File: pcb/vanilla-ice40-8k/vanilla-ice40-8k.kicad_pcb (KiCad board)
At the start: 6 copper layers, 50 x 50 mm, 109 parts, among them J11 QSH-060-01-L-D-A, J12 QSH-060-01-L-D-A, J8 Conn_01x02_Pin, U1 ICE40HX8K-CT256, U2 W25X40CLSN, U3 FT2232HQ, U4 93LCxxBxxOT, U5 TPS563252DRLR, U6 TPS563252DRLR, X1 SG-8101CE 100Mhz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

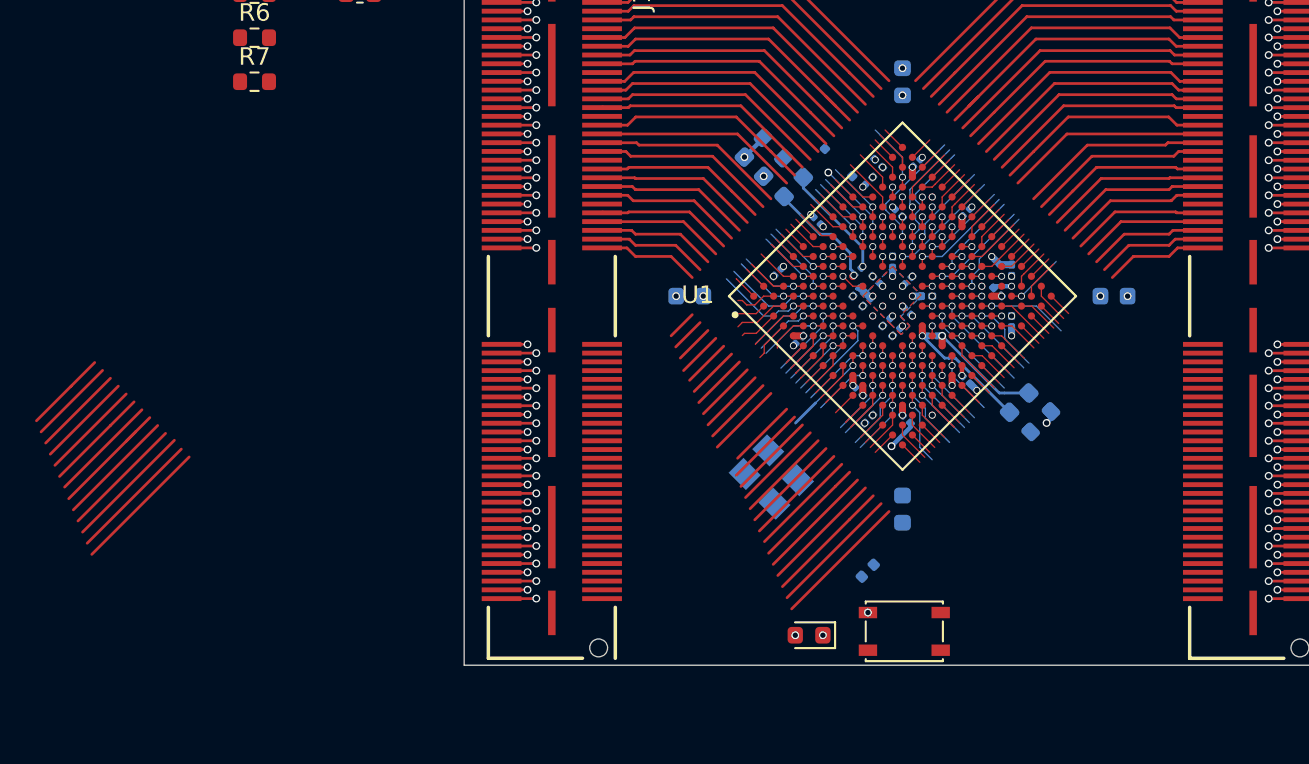
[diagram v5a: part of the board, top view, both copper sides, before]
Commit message: [hx8k][pcb] j1 and j2 mirroring fixed
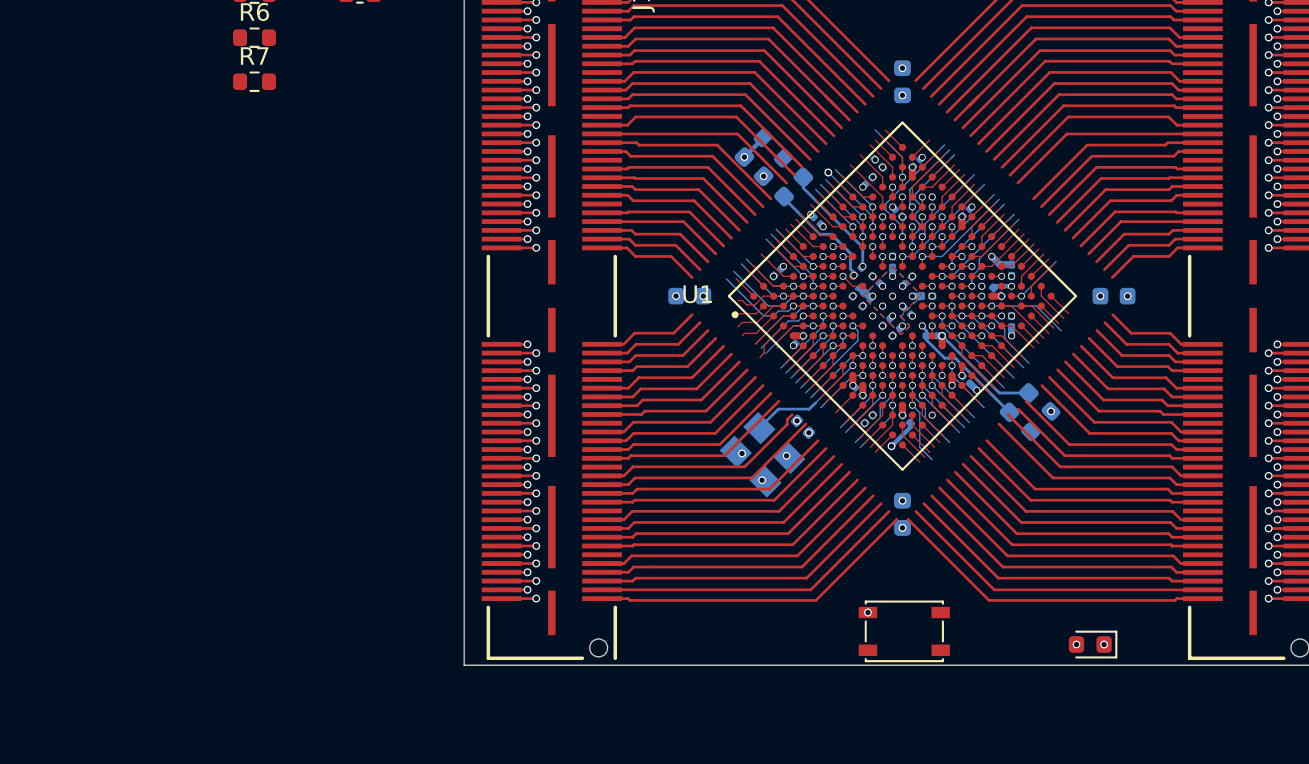
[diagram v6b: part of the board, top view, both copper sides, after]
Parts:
- removed D1: 1N4148WSF-7, Diode_SMD:D_SOD-323F
- moved USR1 16.0 mm to (85.7, 94.9)
- moved C1 9.00 mm to (69.3, 82.5), turned to 135 degrees
- moved X1 1.37 mm to (67.0, 84.0)
- moved C15 0.30 mm to (75.0, 87.4)
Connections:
- C13 pad 1: Net-(D1-K) -> +3V3
- U1 pad E12: Net-(D1-K) -> +3V3
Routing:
- net /IOB_53: track 1.40 -> 20.2 mm
- net /IOB_55: track 2.37 -> 20.6 mm
- net /IOB_57: track 1.40 -> 19.2 mm
- net /IOB_59: track 2.37 -> 19.6 mm
- net /IOB_61: track 1.40 -> 18.2 mm
- net /IOL_24A: track 1.40 -> 18.2 mm
- net /IOB_63: track 2.37 -> 18.5 mm
- net /IOB_60: track 2.37 -> 18.0 mm
- net /IOB_69: track 1.40 -> 16.6 mm
- net /IOB_71: track 2.37 -> 17.1 mm
- net /IOL_17B: track 1.40 -> 16.1 mm
- net unconnected-(J11-Pad110): track 14.1 -> 0.00 mm
- net /IOB_73: track 1.40 -> 15.4 mm
- net /IOB_75: track 1.40 -> 15.0 mm
- net /IOB_76: track 1.40 -> 14.5 mm
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
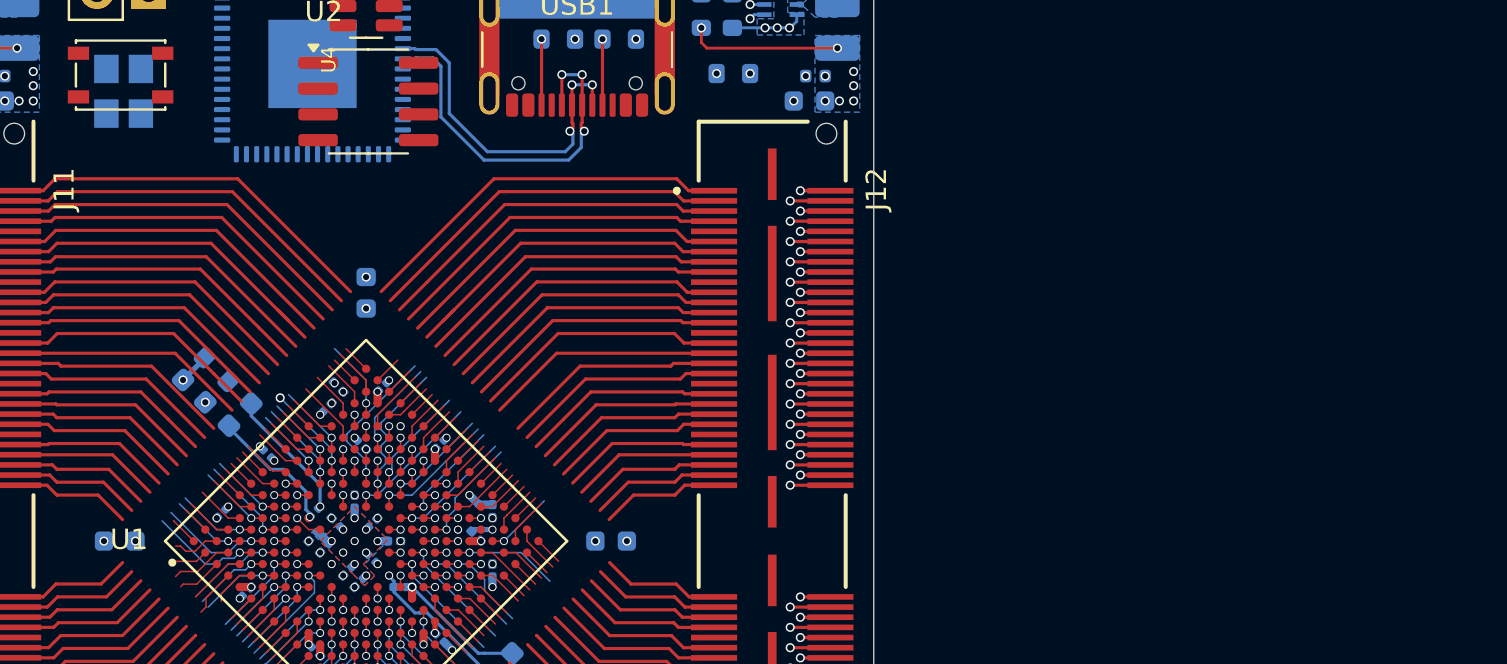
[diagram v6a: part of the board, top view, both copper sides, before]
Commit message: [hx8k][pcb] initial bga to j1 routing
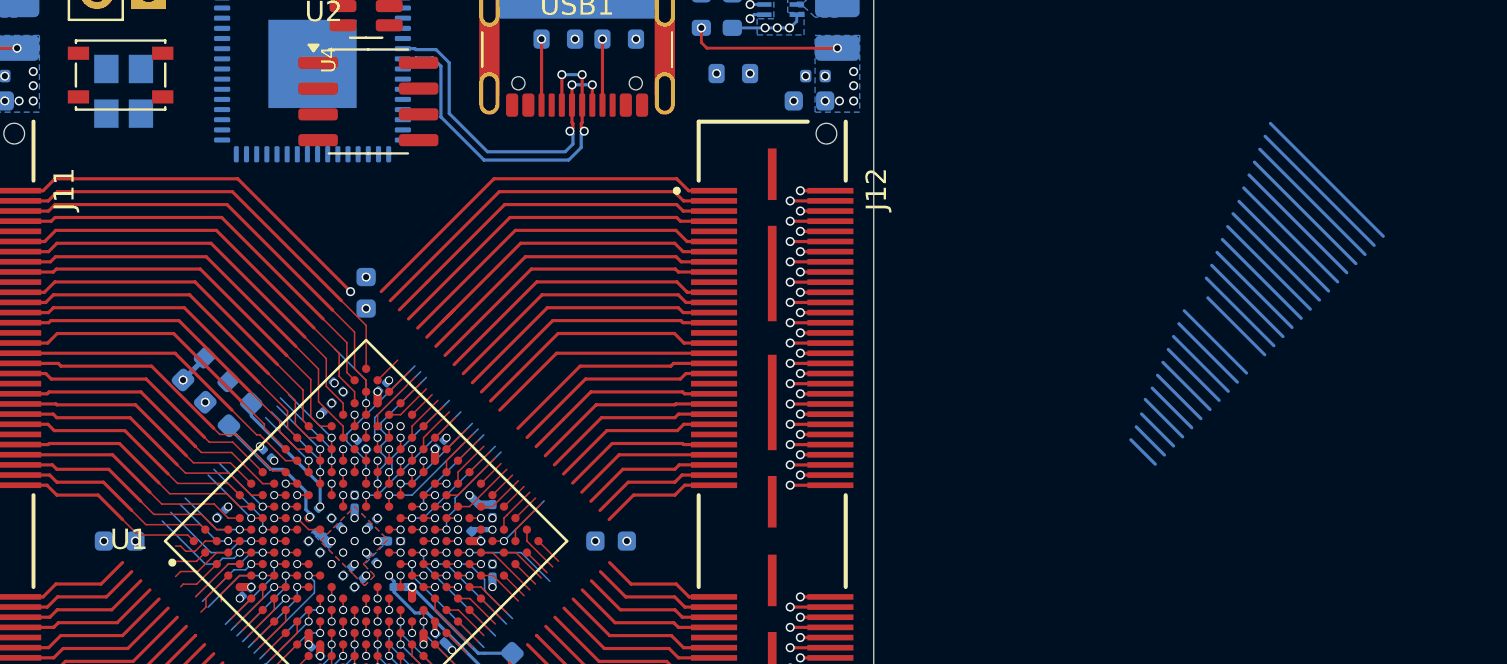
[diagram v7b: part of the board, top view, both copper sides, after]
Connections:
- J11 pad 42: /IOT_208 -> /IOT_207
- J11 pad 44: /IOT_207 -> /IOT_211
- J11 pad 46: /IOT_211 -> /IOT_208
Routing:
- net /IOT_170: track 23.5 -> 34.3 mm, vias 1 -> 2
- net /IOT_176: track 19.8 -> 29.8 mm
- net /IOT_169: track 20.1 -> 29.8 mm
- net /IOT_177: track 18.6 -> 27.9 mm
- net /IOT_171: track 19.2 -> 28.2 mm
- net /IOT_172: track 18.8 -> 27.3 mm
- net /IOT_182: track 17.4 -> 25.8 mm
- net /IOT_187: track 16.1 -> 24.1 mm
- net /IOT_178: track 19.4 -> 27.4 mm
- net /IOT_184: track 17.6 -> 25.3 mm
- net /IOT_186: track 14.9 -> 22.2 mm
- net /IOT_183: track 15.3 -> 22.2 mm
- net /IOT_207: track 11.7 -> 18.3 mm
- net /IOT_194: track 14.0 -> 20.5 mm
- net /IOT_203: track 13.3 -> 19.7 mm
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
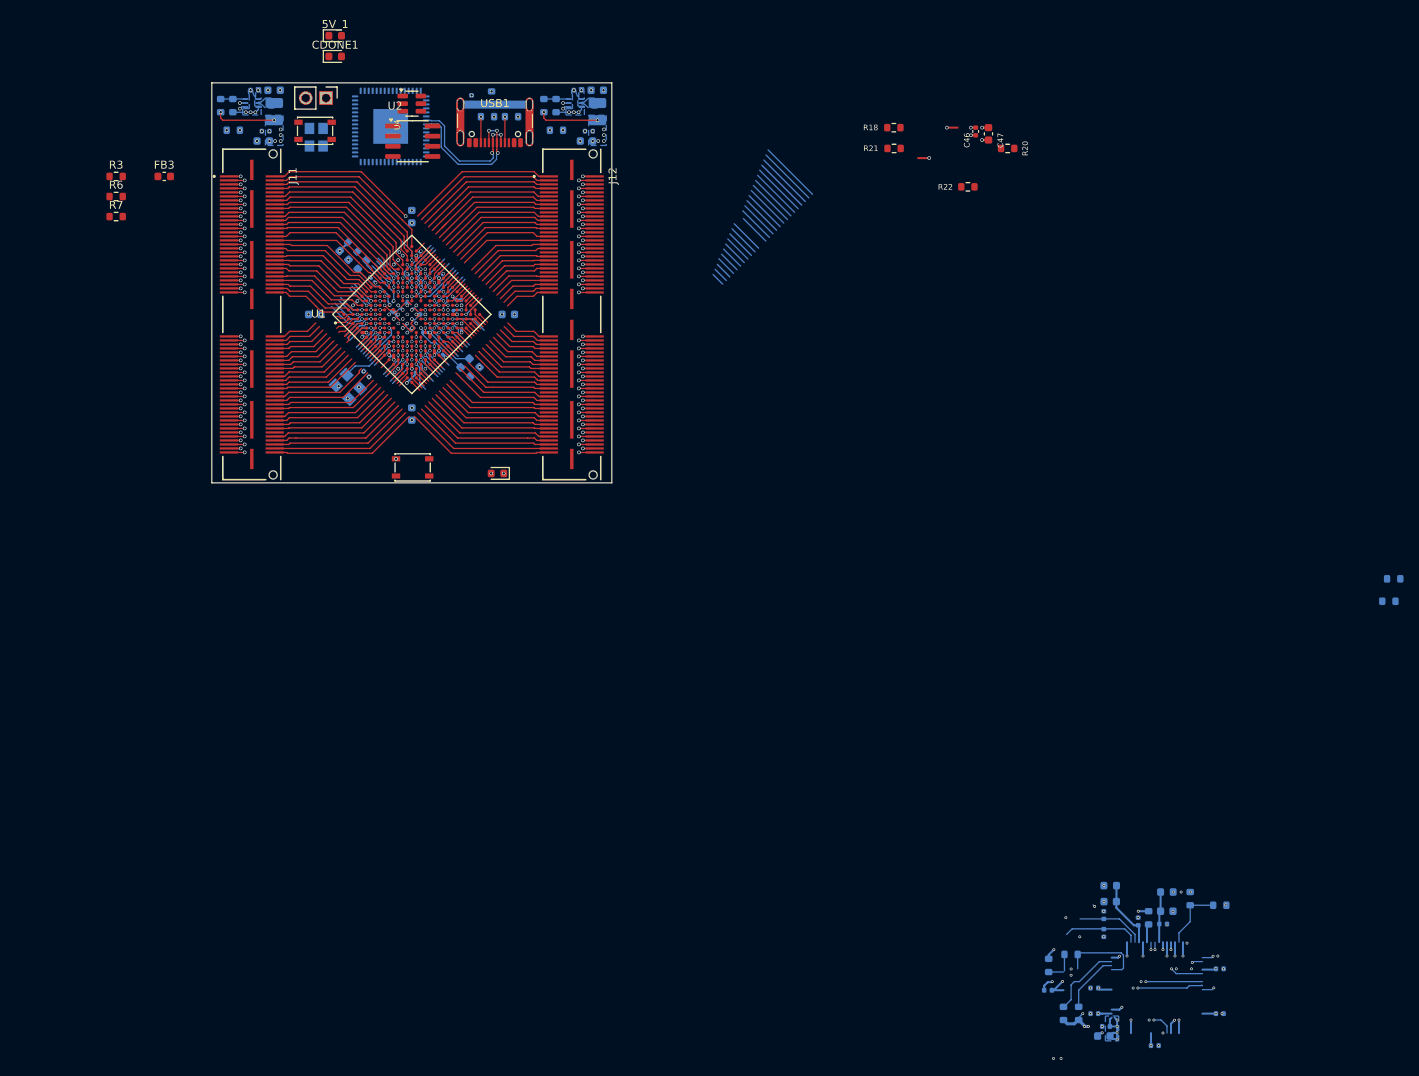
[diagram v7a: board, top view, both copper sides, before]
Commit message: [hx8k][pcb] prep for move to 8 layers
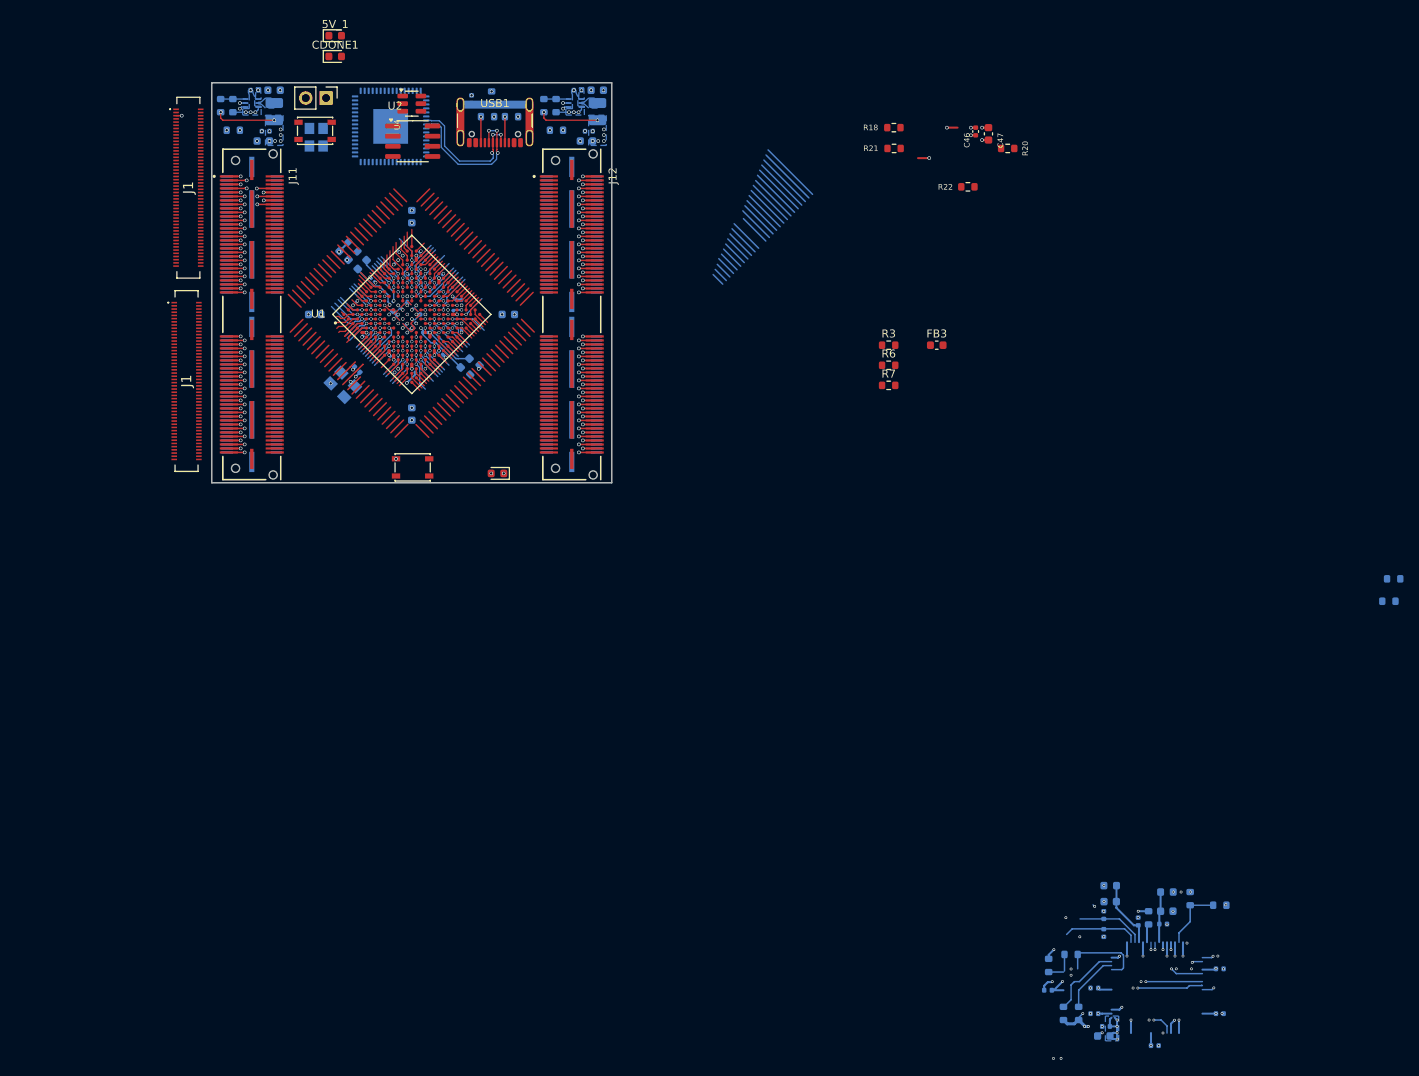
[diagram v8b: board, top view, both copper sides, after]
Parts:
- added J1: DF40C-100DS-0.4V51, DF40C-100DS-0.4V_51:DF40C100DS04V51, F.Cu at (46.8, 83.3)
- added J1: DF40C-100DS-0.4V51, DF40C-100DS-0.4V_51:DF40C100DS04V51, F.Cu at (47.1, 59.2)
- added J1: QTH-060-01-L-D-A, !Misc:SAMTEC_QTH-060-01-X-D-A, B.Cu at (95.0, 75.0)
- added J2: QTH-060-01-L-D-A, !Misc:SAMTEC_QTH-060-01-X-D-A, B.Cu at (55.0, 75.0)
- moved FB3 98.8 mm to (140.6, 78.8)
- moved R3 98.8 mm to (134.6, 78.8)
- moved R6 98.8 mm to (134.6, 81.4)
- moved R7 98.8 mm to (134.6, 83.9)
- moved C1 1.27 mm to (68.2, 81.9)
- moved X1 0.68 mm to (66.4, 83.8)
- moved R10 0.22 mm to (82.9, 81.9)
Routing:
- net /IOB_52: track 6.01 -> 118.5 mm
- net /IOB_54: track 5.63 -> 110.5 mm
- net /IOT_176: track 29.8 -> 9.73 mm
- net /IOT_169: track 29.8 -> 10.5 mm
- net /IOT_170: track 34.3 -> 15.4 mm, vias 2 -> 1
- net /IOR_165: track 20.3 -> 1.40 mm
- net /IOB_53: track 20.2 -> 1.40 mm
- net /IOL_25B: track 25.1 -> 6.30 mm
- net /IOR_161: track 19.8 -> 1.40 mm
- net /IOL_23B: track 22.0 -> 3.73 mm
- net /IOB_55: track 20.6 -> 2.37 mm
- net /IOR_167: track 20.9 -> 3.17 mm
- net /IOB_57: track 19.2 -> 1.40 mm
- net /IOL_26A: track 19.2 -> 1.40 mm
- net /IOB_59: track 19.6 -> 2.37 mm
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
